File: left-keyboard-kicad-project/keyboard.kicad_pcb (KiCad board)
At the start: 2 copper layers, 180 x 155.4 mm, 78 parts, among them U1 Arduino_Pro_Micro, U2 TRRS

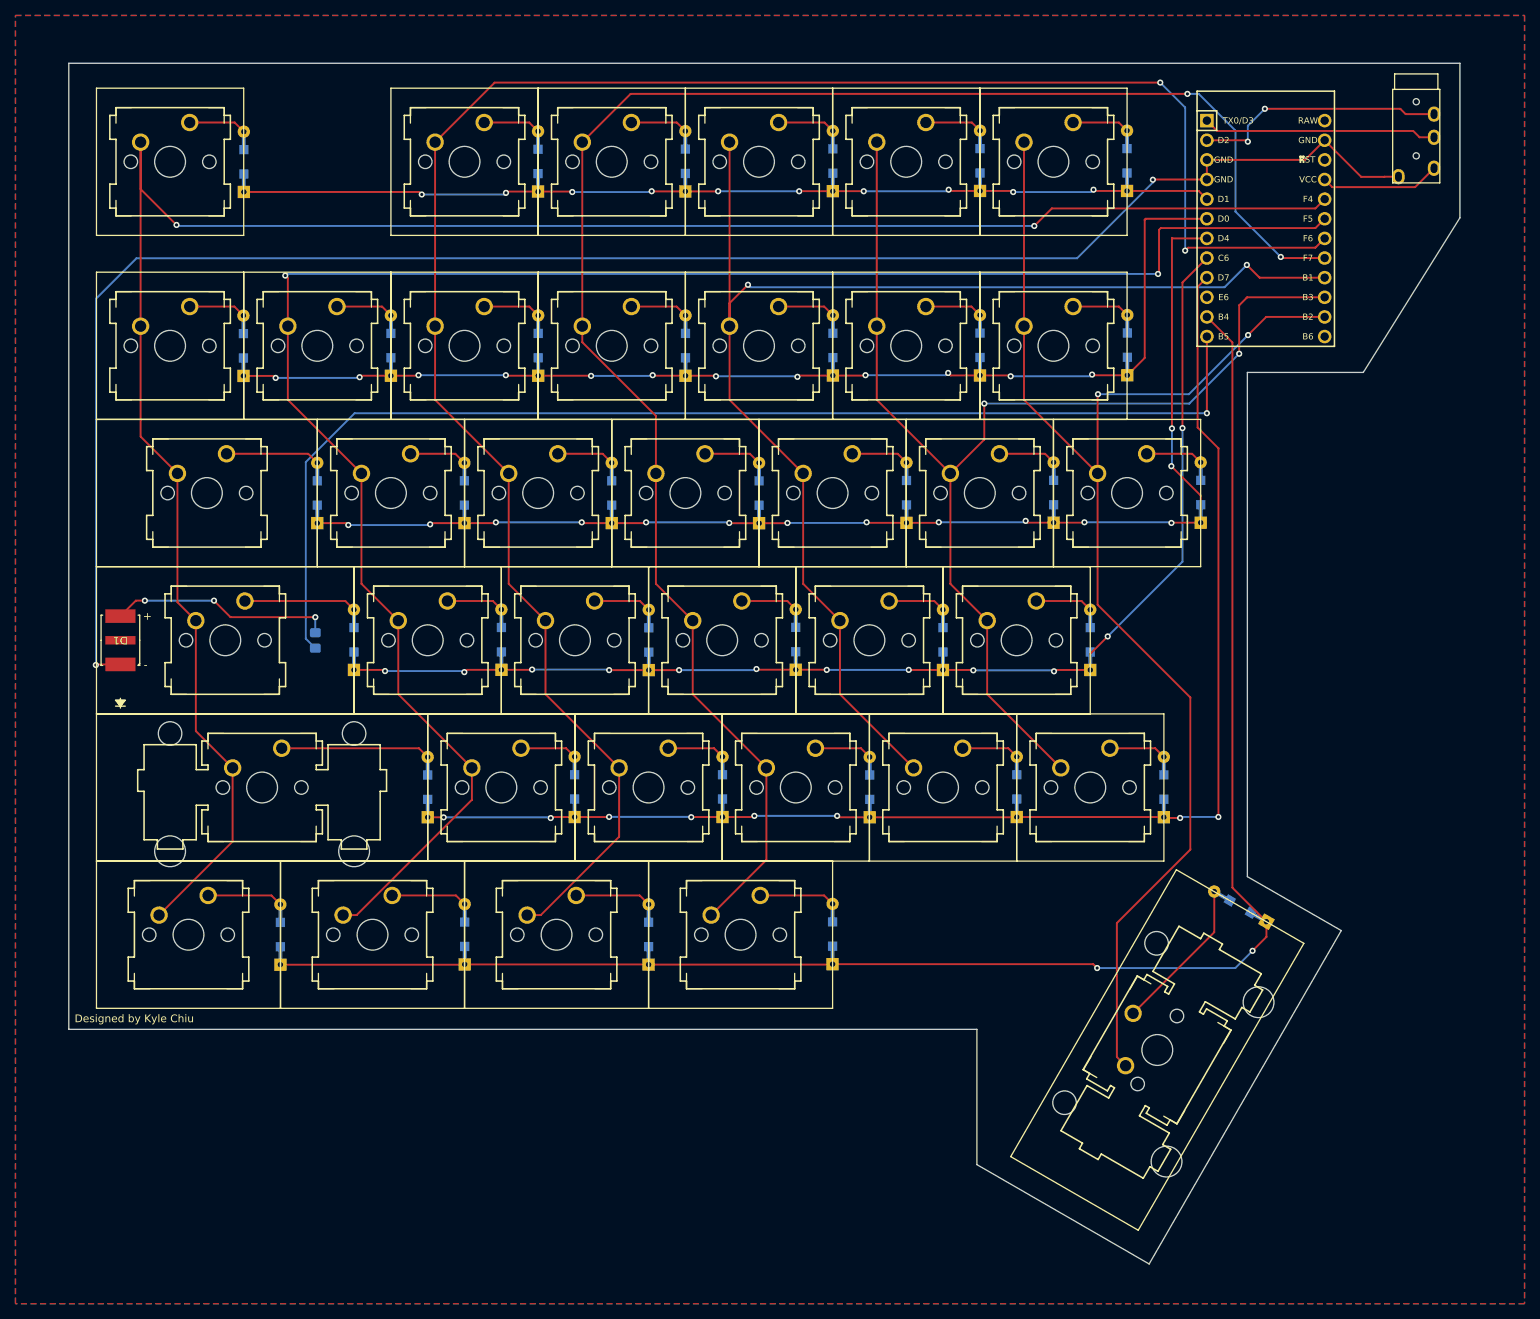
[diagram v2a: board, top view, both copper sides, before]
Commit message: added hotswap sockets
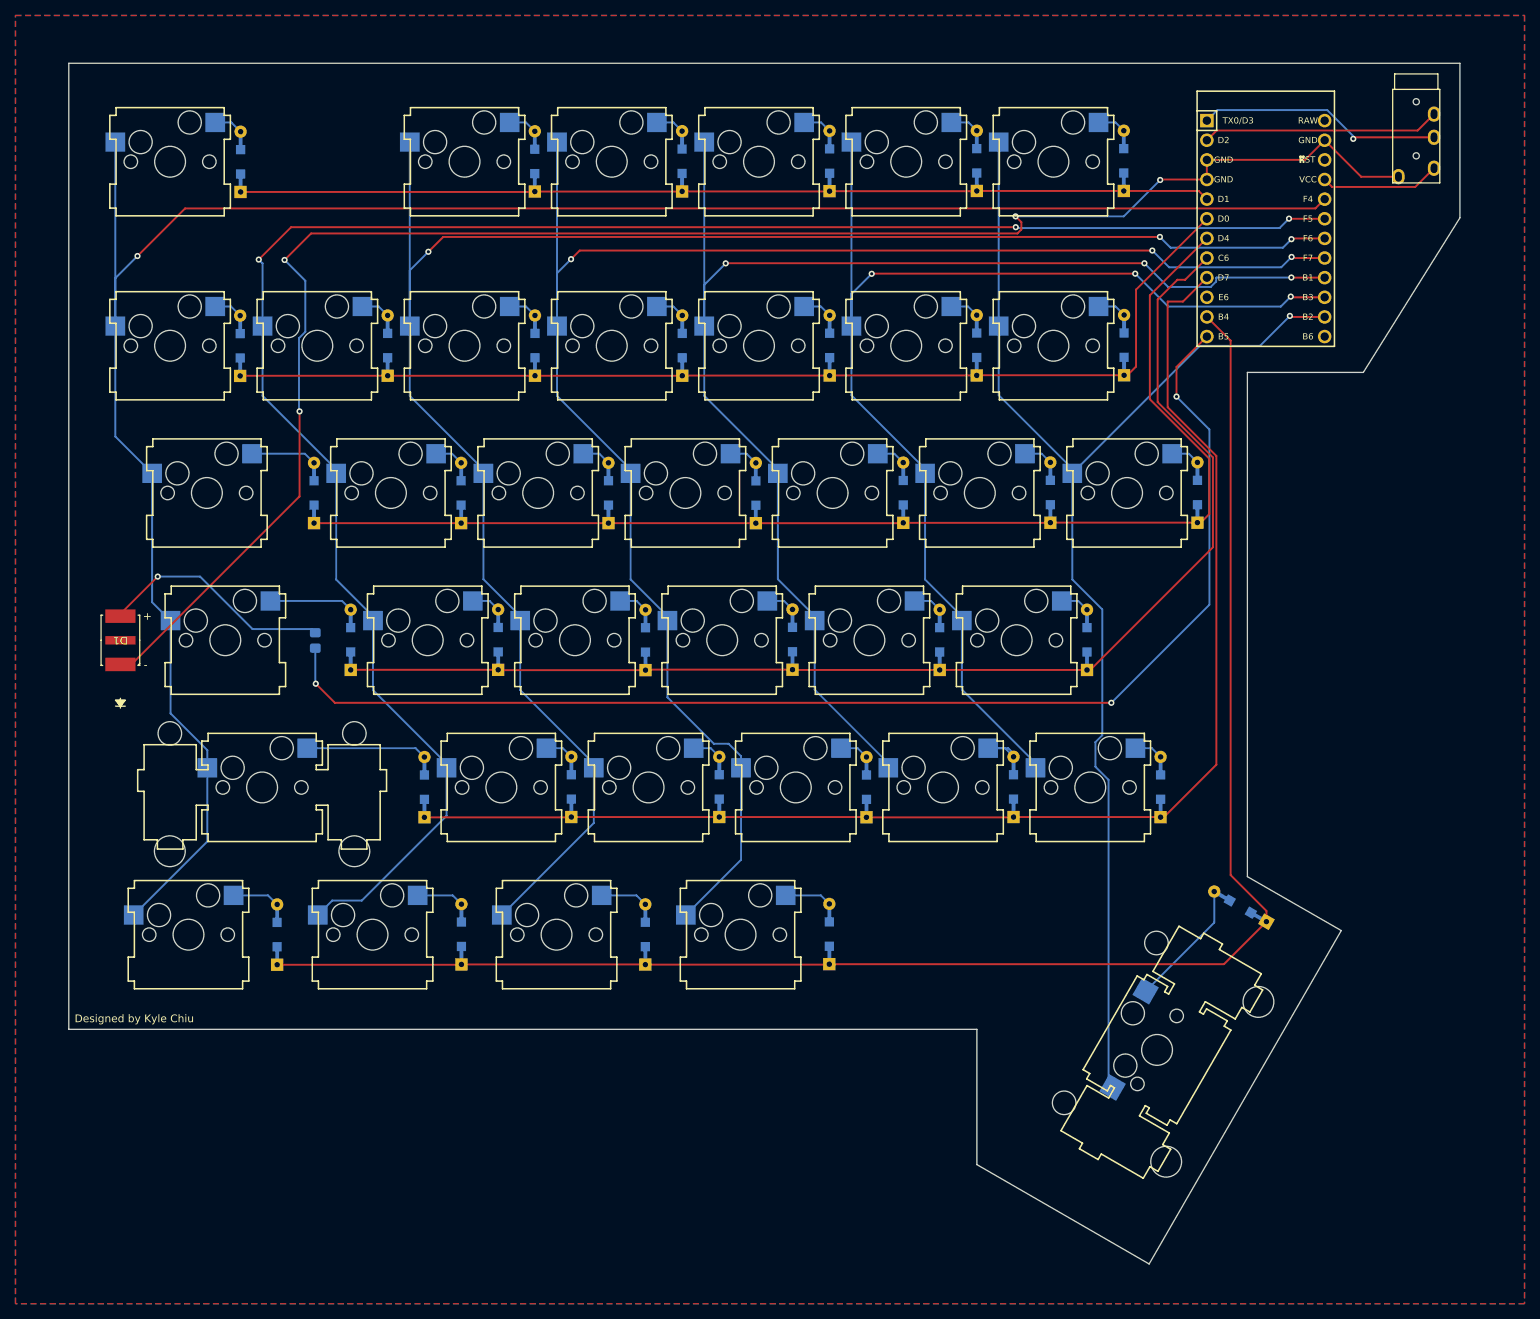
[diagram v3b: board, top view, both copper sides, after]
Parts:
- K_1, K_2, K_3, K_4, K_5, K_6, K_A1, K_B1, K_C1, K_D1, K_E1, K_ESC1, K_F1, K_F2, K_F3, K_F4, K_F5, K_F6, K_G1, K_Q1, K_R1, K_S1, K_T1, K_V1, K_W1, K_X1, K_Y1, K_Z1, K_`1: footprint MX_ALPS_Hybrid:MXOnly-1U-NoLED -> MX_Alps_Hybrid_3:MXOnly-1U-Hotswap
- K_ALT1, K_CTRL1, K_FN1, K_WIN1: footprint MX_ALPS_Hybrid:MXOnly-1.25U-NoLED -> MX_Alps_Hybrid_3:MXOnly-1.25U-Hotswap
- K_CAPS1: footprint MX_ALPS_Hybrid:MXOnly-1.75U-NoLED -> MX_Alps_Hybrid_3:MXOnly-1.75U-Hotswap
- K_SHIFT1, K_SPACE1: footprint MX_ALPS_Hybrid:MXOnly-2.25U-NoLED -> MX_Alps_Hybrid_3:MXOnly-2.25U-Hotswap
- K_TAB1: footprint MX_ALPS_Hybrid:MXOnly-1.5U-NoLED -> MX_Alps_Hybrid_3:MXOnly-1.5U-Hotswap
- moved D_4 0.42 mm to (143.4, 66.5)
- moved D_5 0.42 mm to (162.5, 66.5)
- moved D_F3 0.42 mm to (143.4, 42.6)
- moved D_F5 0.42 mm to (181.5, 42.6)
- moved D_FN1 0.42 mm to (143.4, 142.7)
- moved D_R1 0.42 mm to (153.0, 85.6)
- moved D_T1 0.42 mm to (172.0, 85.5)
- moved D_X1 0.42 mm to (129.2, 123.6)
- moved D_Y1 0.42 mm to (191.0, 85.5)
- moved D_1 0.42 mm to (86.3, 66.5)
- moved D_2 0.42 mm to (105.3, 66.5)
- moved D_3 0.42 mm to (124.4, 66.5)
- moved D_A1 0.42 mm to (100.6, 104.6)
- moved D_CTRL1 0.42 mm to (72.0, 142.7)
- moved D_ESC1 0.42 mm to (67.2, 42.8)
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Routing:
- net col2: track 254.6 -> 243.3 mm, vias 2 -> 3
- net GND: track 231.3 -> 220.3 mm, vias 2 -> 4
- net Net-(U1-9/PB5): track 153.7 -> 164.6 mm, vias 1 -> 3
- net col6: track 176.6 -> 170.3 mm, vias 2 -> 1
- net row3: track 155.4 -> 161.4 mm, vias 12 -> 0
- net col4: track 173.8 -> 179.7 mm, vias 2 -> 3
- net row1: track 144.5 -> 138.9 mm, vias 12 -> 0
- net col5: track 155.1 -> 159.6 mm, vias 2 -> 3
- net col0: track 271.6 -> 275.8 mm, vias 2 -> 1
- net Net-(D_T1-A): track 7.47 -> 3.75 mm
- net Net-(D_C1-A): track 7.50 -> 3.78 mm
- net Net-(D_SHIFT1-A): track 19.4 -> 15.6 mm
- net Net-(D_Q1-A): track 7.45 -> 3.73 mm
- net Net-(D_ESC1-A): track 7.49 -> 3.77 mm
- net Net-(D_1-A): track 7.46 -> 3.74 mm
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
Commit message: Moved MCU and redid board cuts
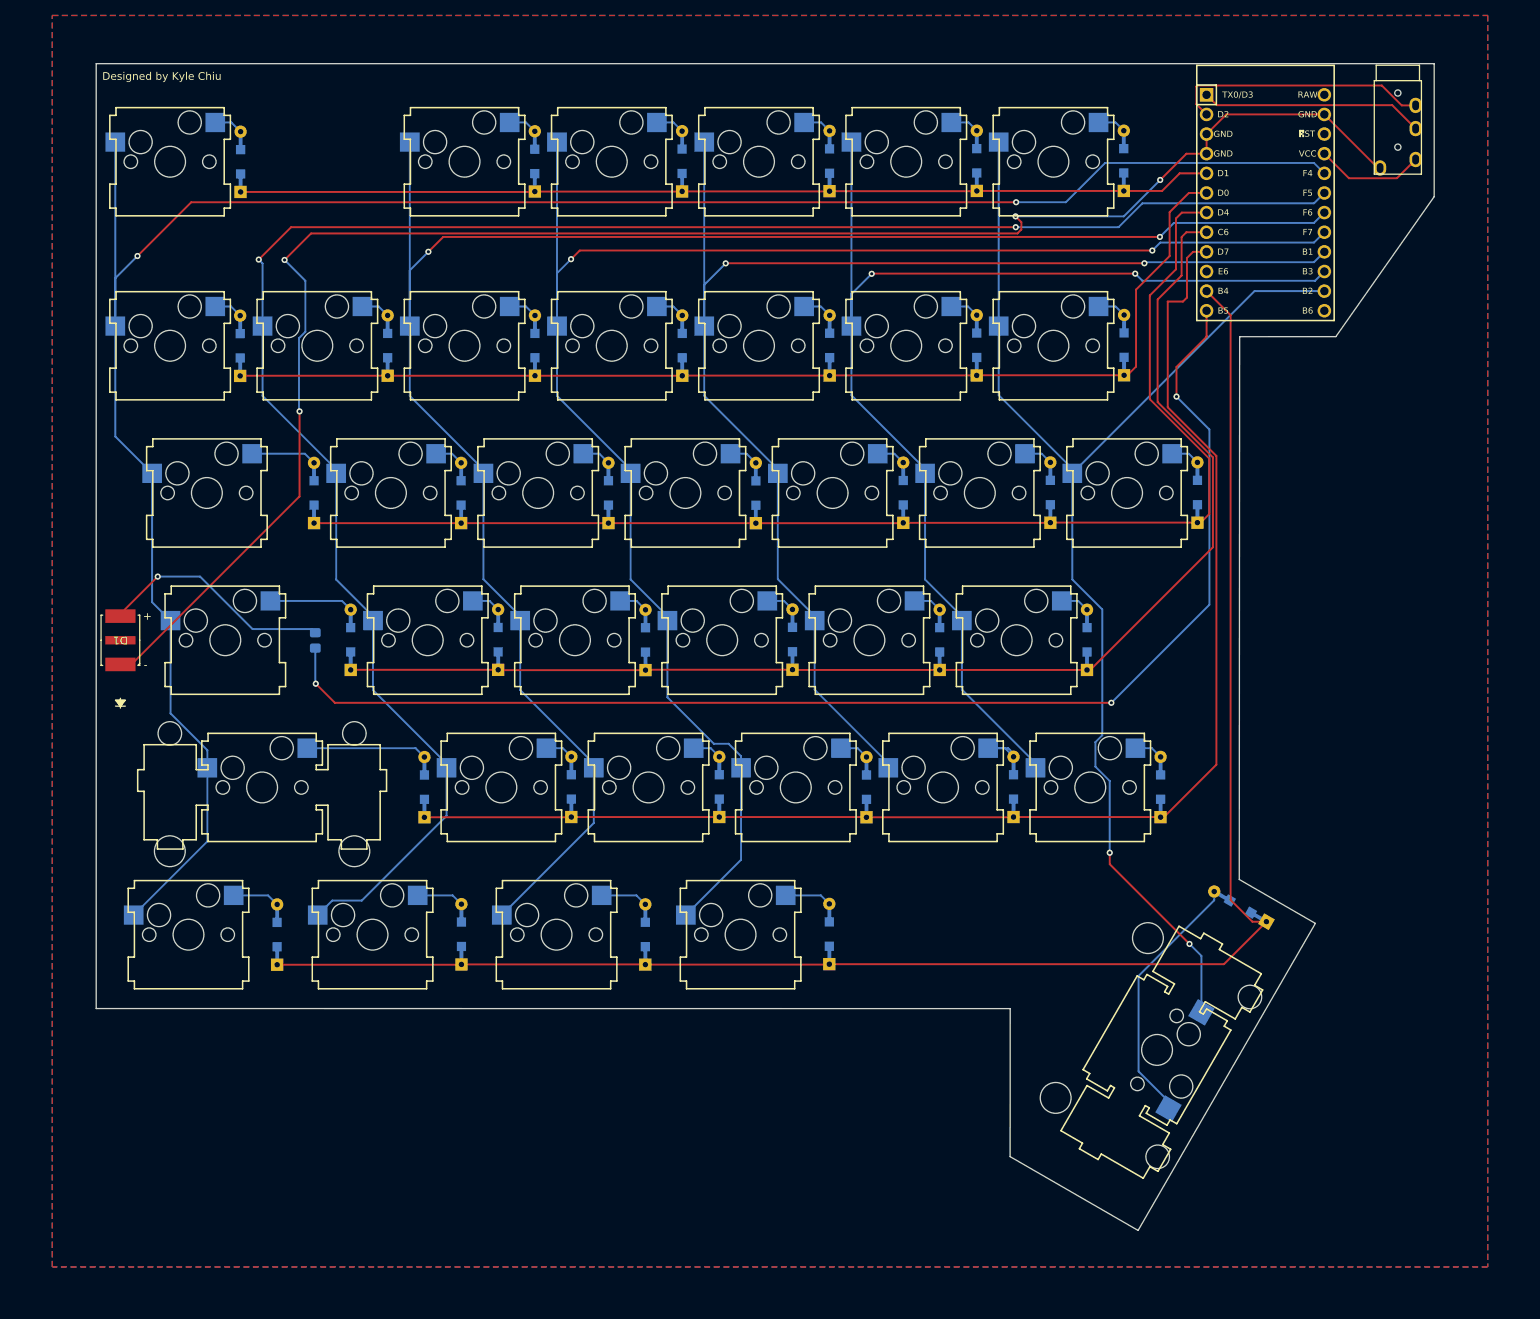
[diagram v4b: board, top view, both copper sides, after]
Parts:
- moved U1 3.34 mm to (199.8, 48.0)
- moved U2 2.63 mm to (217.0, 32.2)
- turned K_SPACE1 to -120 degrees
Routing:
- net Net-(D_SPACE1-A): track 16.6 -> 33.7 mm
- net row2: track 157.8 -> 163.0 mm
- net row1: track 138.9 -> 143.6 mm
- net row5: track 211.4 -> 215.8 mm
- net row4: track 173.8 -> 178.1 mm
- net row3: track 161.4 -> 165.7 mm
- net col6: track 170.3 -> 166.6 mm, vias 1 -> 2
- net Net-(U1-9/PB5): track 164.6 -> 168.0 mm
- net Net-(U1-TX0/PD3): track 31.8 -> 28.9 mm, vias 1 -> 0
- net Net-(U1-RX1/PD2): track 30.8 -> 33.7 mm
- net col0: track 275.8 -> 278.3 mm, vias 1 -> 2
- net col5: track 159.6 -> 158.1 mm, vias 3 -> 2
- net col4: track 179.7 -> 178.2 mm, vias 3 -> 2
- net Net-(U1-VCC): track 15.6 -> 14.1 mm
- net col1: track 244.2 -> 245.6 mm, vias 3 -> 2
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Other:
- board size 180 x 155.4 mm -> 173.1 x 151 mm

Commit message: Updated track width for VCC to be thicker
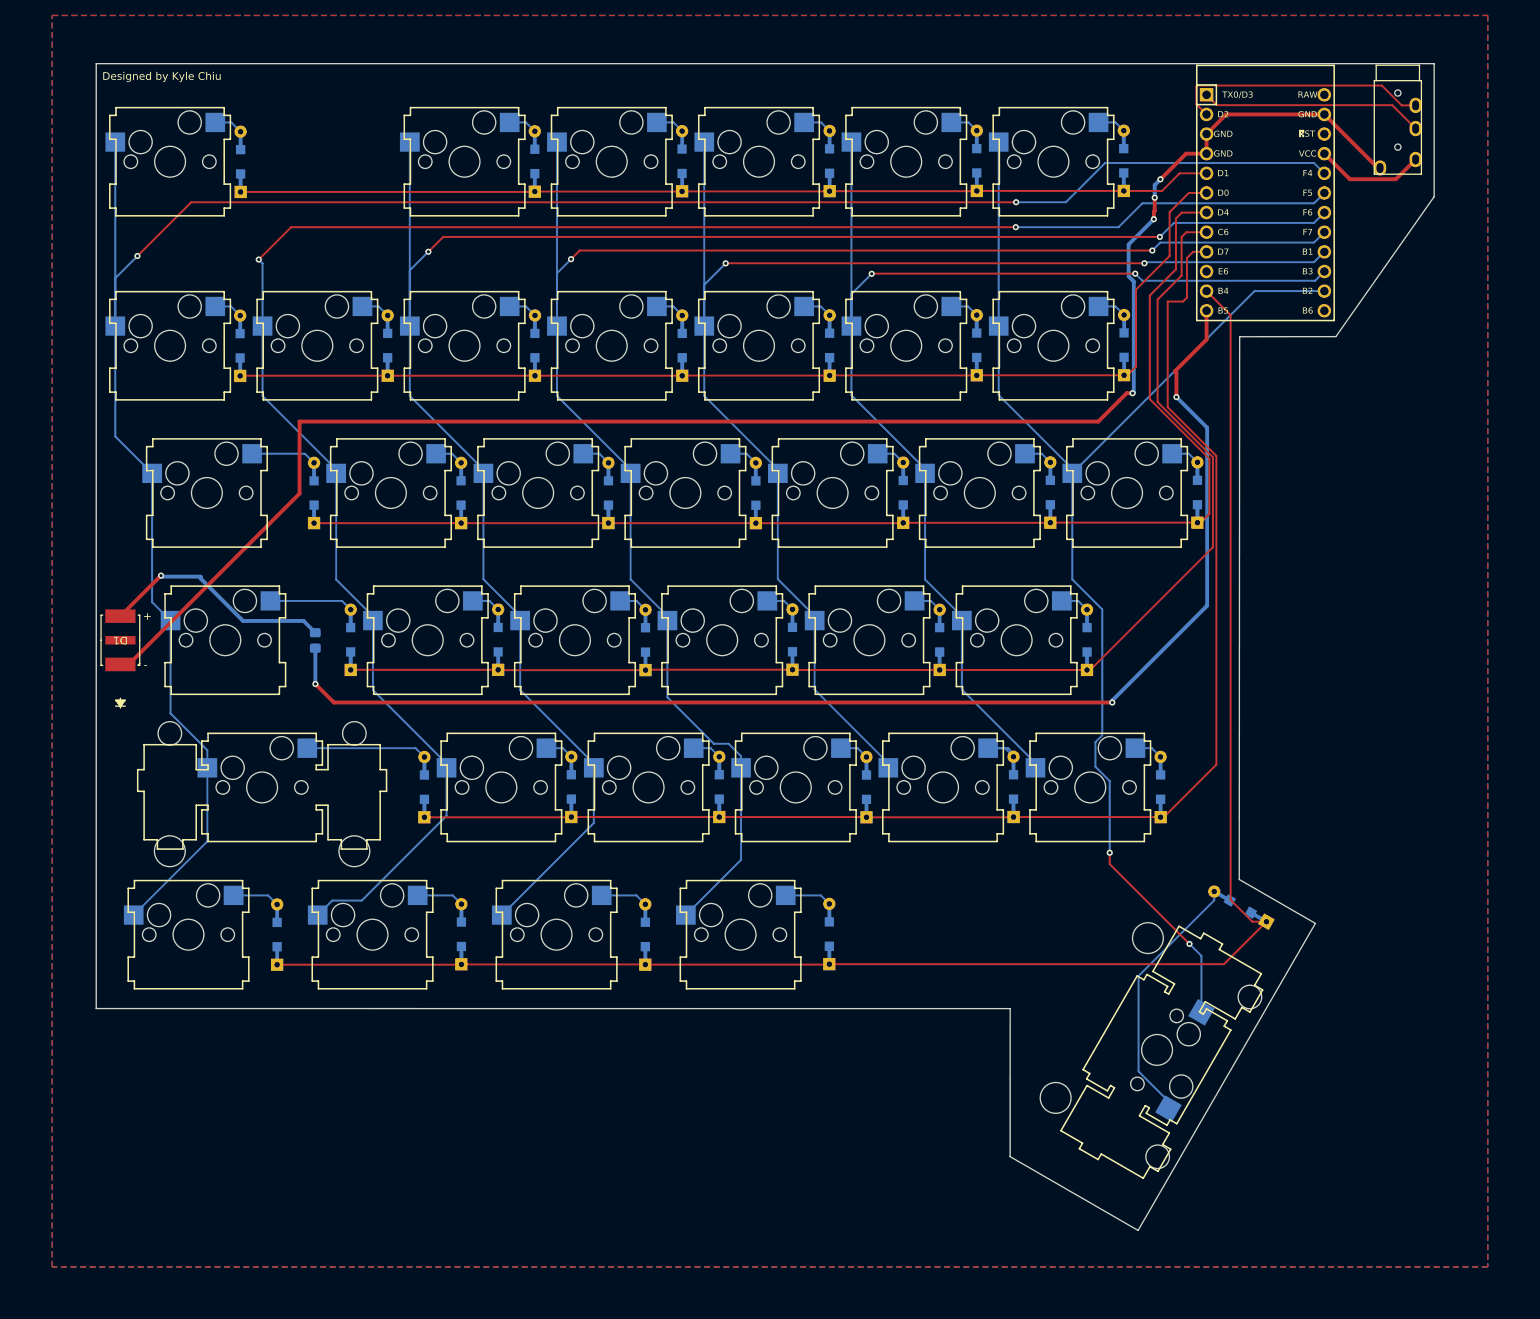
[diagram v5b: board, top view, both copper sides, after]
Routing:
- net GND: track 220.2 -> 218.4 mm
- net Net-(D1-A): track 30.5 -> 31.5 mm

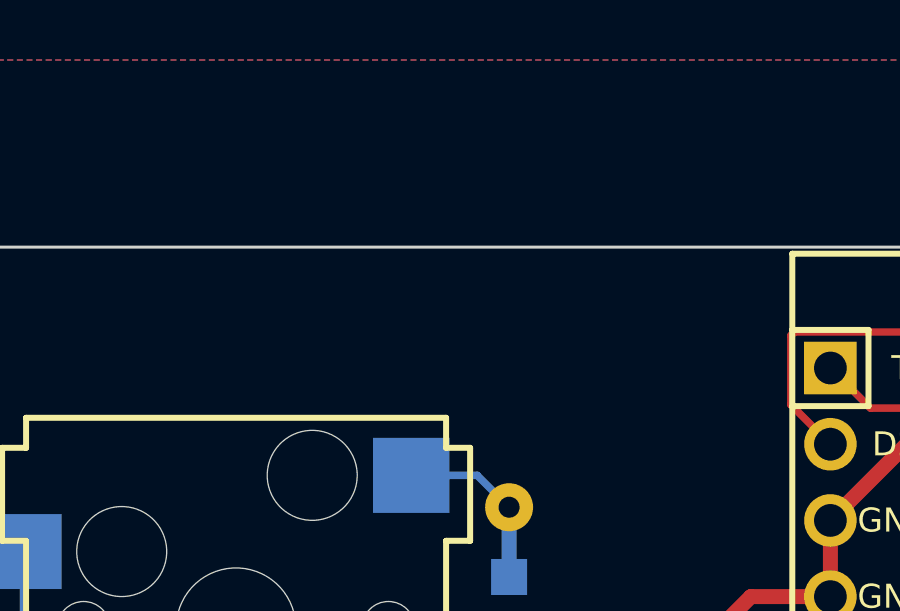
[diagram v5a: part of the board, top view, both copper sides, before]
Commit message: Generated gerber files for both left and right keyboards
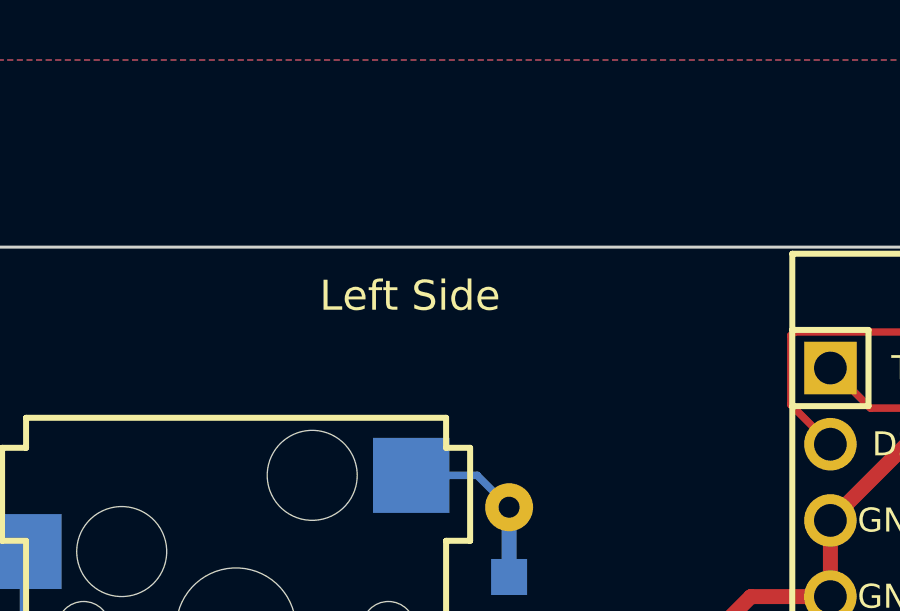
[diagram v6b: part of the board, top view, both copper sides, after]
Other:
- board text added: "Left Side"
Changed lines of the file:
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@@
+    (effects (font (size 1 1) (thickness 0.15)) (justify left bottom))
+  )
+  (gr_text "Left Side" (at 175.19 32.26) (layer "F.SilkS")
     (effects (font (size 1 1) (thickness 0.15)) (justify left bottom))
   )
